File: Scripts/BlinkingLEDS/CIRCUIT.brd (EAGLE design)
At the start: 68.6 x 53.3 mm, 11 parts

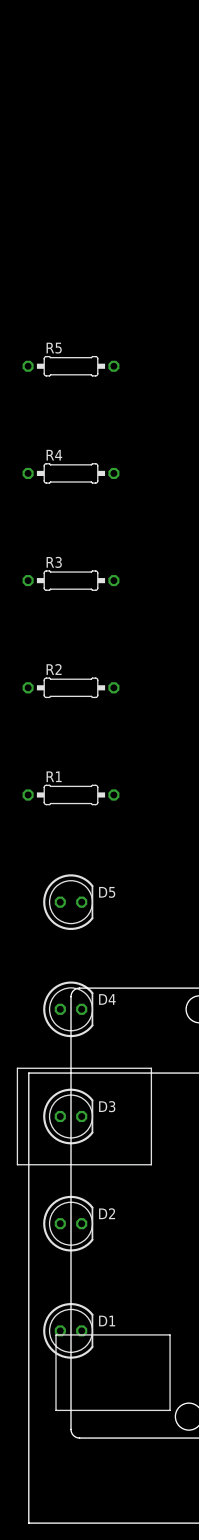
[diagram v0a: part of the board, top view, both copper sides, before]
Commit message: added an lcd to display time
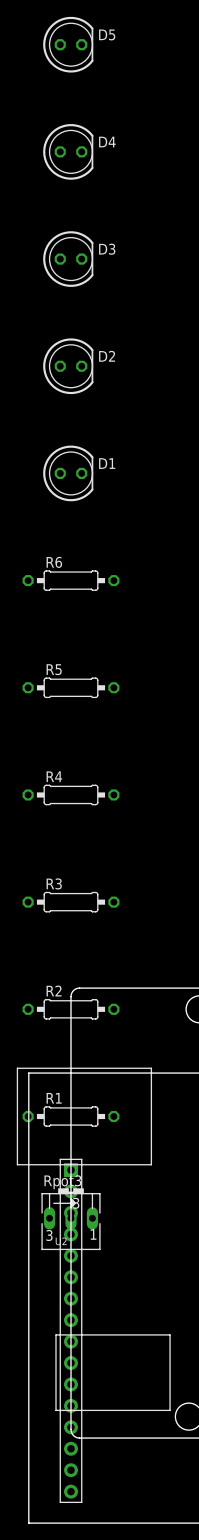
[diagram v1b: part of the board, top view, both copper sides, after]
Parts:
- added R6: 1k‎Ω, AUTODESK_CIRCUITS_BREADBOARD:0207/10
- added Rpot3: 250k‎Ω, AUTODESK_CIRCUITS_BREADBOARD:B25V
- added U2: (no value), AUTODESK_CIRCUITS_BREADBOARD:1X16P-2.54-2.54-11.6-3.0-BLACK-MALE
- R1: value 1k‎Ω -> 220‎Ω
- moved D5 101.6 mm to (5.00, 175.2)
- moved D4 101.6 mm to (5.00, 162.5)
- moved D3 101.6 mm to (5.00, 149.8)
- moved D1 101.6 mm to (5.00, 124.4)
- moved D2 101.6 mm to (5.00, 137.1)
- moved R2 38.1 mm to (5.00, 60.9)
- moved R3 38.1 mm to (5.00, 73.6)
- moved R4 38.1 mm to (5.00, 86.3)
- moved R5 38.1 mm to (5.00, 99.0)
- moved R1 38.1 mm to (5.00, 48.2)
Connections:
- new net N$12: R2.1, U1.10
- new net N$13: D2.A, R3.2
- new net N$14: R3.1, U1.9
- new net N$15: D3.A, R4.2
- new net N$16: R4.1, U1.8
- new net N$17: D4.A, R5.2
- new net N$18: R5.1, U1.7
- new net N$19: D5.A, R6.2
- new net N$20: R6.1, U1.6
- new net N$21: D1.K, D2.K, D3.K, D4.K, D5.K, U1.GND
- net N$1: now also Rpot3.E, U1.GND.., U2.1, U2.16, U2.5; no longer D2.A, R2.2
- net N$10: now also R1.1, Rpot3.A, U1.5V, U2.2; no longer R4.1, U1.5
- net N$11: now also D1.A, R2.2; no longer R5.1, U1.6
- net N$2: now also U1.12, U2.4; no longer D3.A, R3.2
- net N$3: now also U1.11, U2.6; no longer D4.A, R4.2
- net N$4: now also U1.5, U2.11; no longer D1.K, D2.K, D3.K, D4.K, D5.K, U1.GND.
- net N$5: now also U1.4, U2.12; no longer D5.A, R5.2
- net N$6: now also U1.3, U2.13; no longer D1.A, R1.2
- net N$7: now also U2.14; no longer R1.1
- net N$8: now also Rpot3.S, U2.3; no longer R2.1, U1.3
- net N$9: now also R1.2, U2.15; no longer R3.1, U1.4
